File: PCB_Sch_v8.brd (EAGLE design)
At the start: 38.3 x 38.1 mm, 60 parts, among them IC1 CP2104, M1 C0720B001F, Q1 MMBT2222LT1G, Q2 mmbt2222, Q3 DMG3415U, Q4 mmbt2222, U1 ESP32-WROOM-32D, U2 UG-2828GDEDF11, U3 MCP73831T-2ACI/OT, U4 AP2112-3.3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

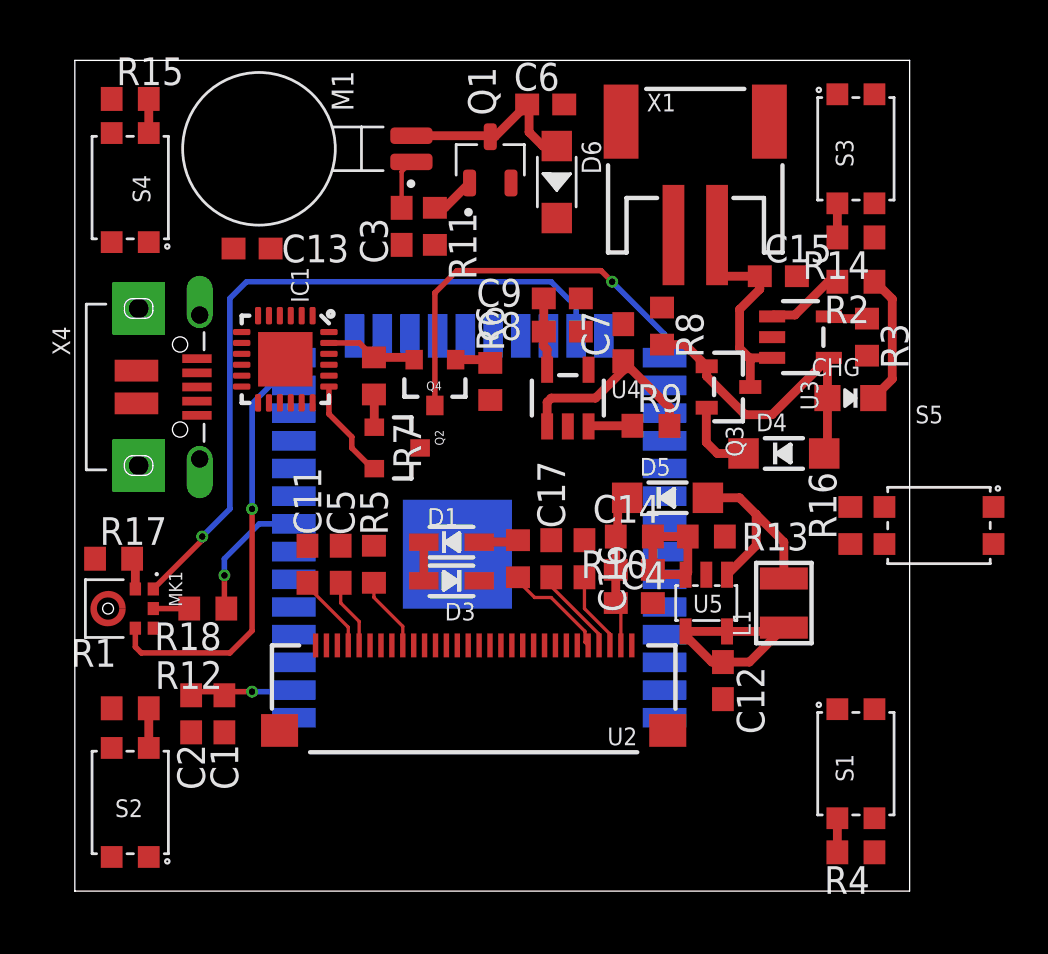
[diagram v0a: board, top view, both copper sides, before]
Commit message: Started routing, made some fixes
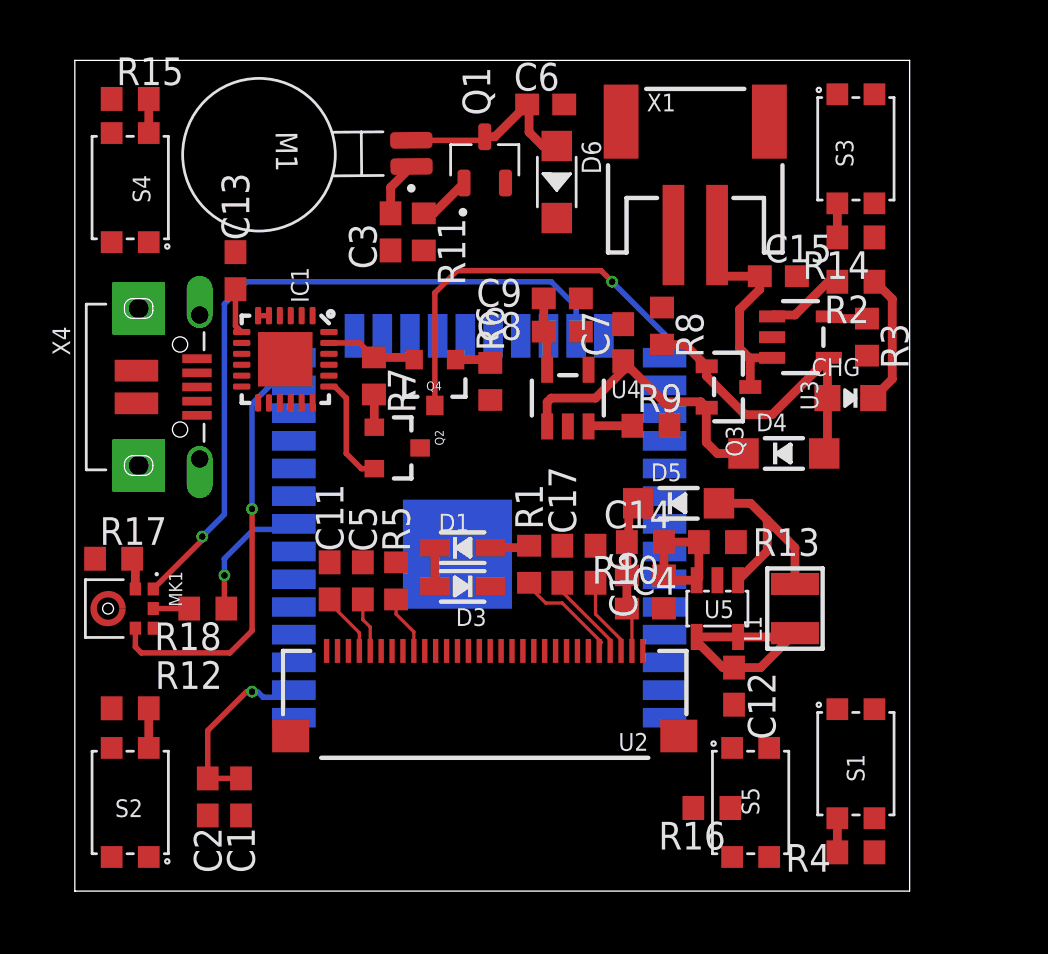
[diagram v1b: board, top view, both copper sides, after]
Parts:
- moved S5 15.4 mm to (31.0, 4.06), turned to 90 degrees
- moved R16 14.4 mm to (29.2, 3.81), turned to 180 degrees
- moved C1 3.89 mm to (7.62, 4.32)
- moved C2 3.89 mm to (6.10, 4.32)
- moved C11 1.27 mm to (11.7, 14.2)
- moved C5 1.27 mm to (13.2, 14.2)
- moved R5 1.27 mm to (14.7, 14.2)
- moved C13 1.27 mm to (7.37, 28.4), turned to 90 degrees
- moved R11 0.57 mm to (16.0, 30.2)
- moved C16 0.57 mm to (23.9, 15.0)
- moved D1 0.57 mm to (17.8, 15.7)
- moved D3 0.57 mm to (17.8, 14.0)
- moved L1 0.57 mm to (33.0, 13.0)
- moved C3 0.57 mm to (14.5, 30.2)
- moved R10 0.57 mm to (26.2, 16.0)
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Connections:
- removed net OUT: C8.1, C9.1, U4.5
- net 3.3V: now also C8.1, C9.1, U4.5
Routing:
- net 3.3V: track 24.3 -> 34.2 mm
- net OUT: track 3.34 -> 0.00 mm
- net N$12: track 13.0 -> 15.1 mm
- net VBAT: track 10.5 -> 8.73 mm
- net N$19: track 3.42 -> 2.70 mm
- net N$3: track 3.22 -> 2.50 mm
